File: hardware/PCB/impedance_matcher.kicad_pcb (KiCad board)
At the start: 2 copper layers, 72 x 63 mm, 43 parts, among them Q1 PC817, U1 TLV2372IP

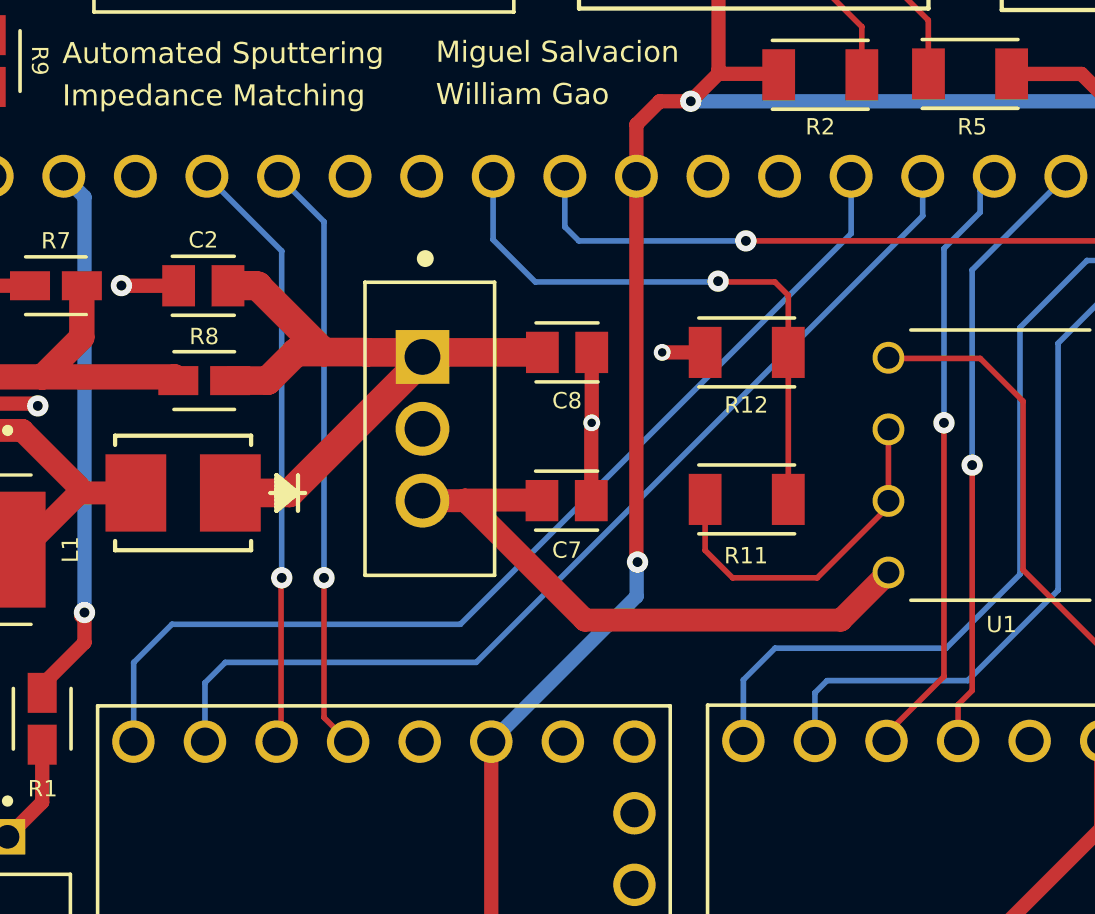
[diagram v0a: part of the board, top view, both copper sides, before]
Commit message: Move capacitor closer to op-amp VDD
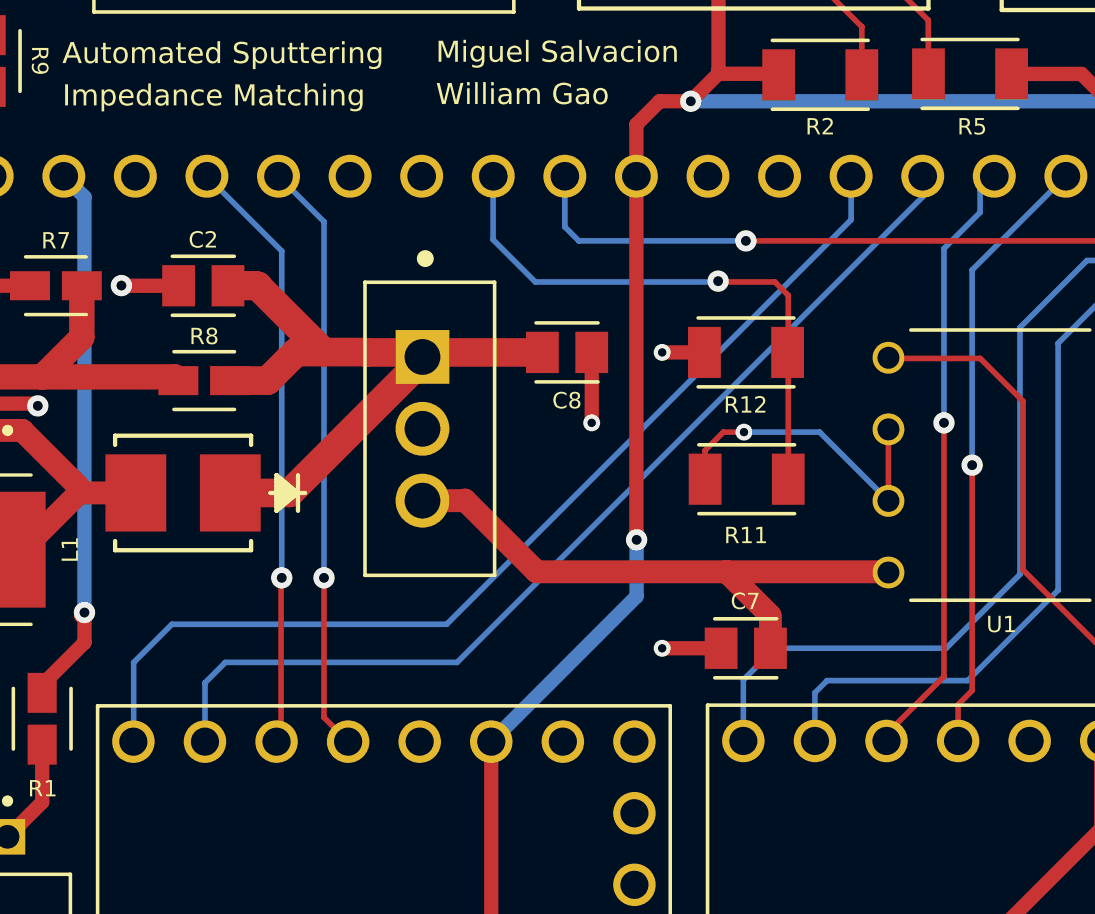
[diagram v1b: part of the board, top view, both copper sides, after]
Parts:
- moved C7 8.24 mm to (69.5, 57.0), turned to 0 degrees
- moved R11 0.72 mm to (69.5, 51.0)
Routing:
- net /IN2: track 12.3 -> 11.3 mm, vias 0 -> 1
- net 12V: track 21.6 -> 20.9 mm
- net GND: track 24.6 -> 24.0 mm, vias 9 -> 10

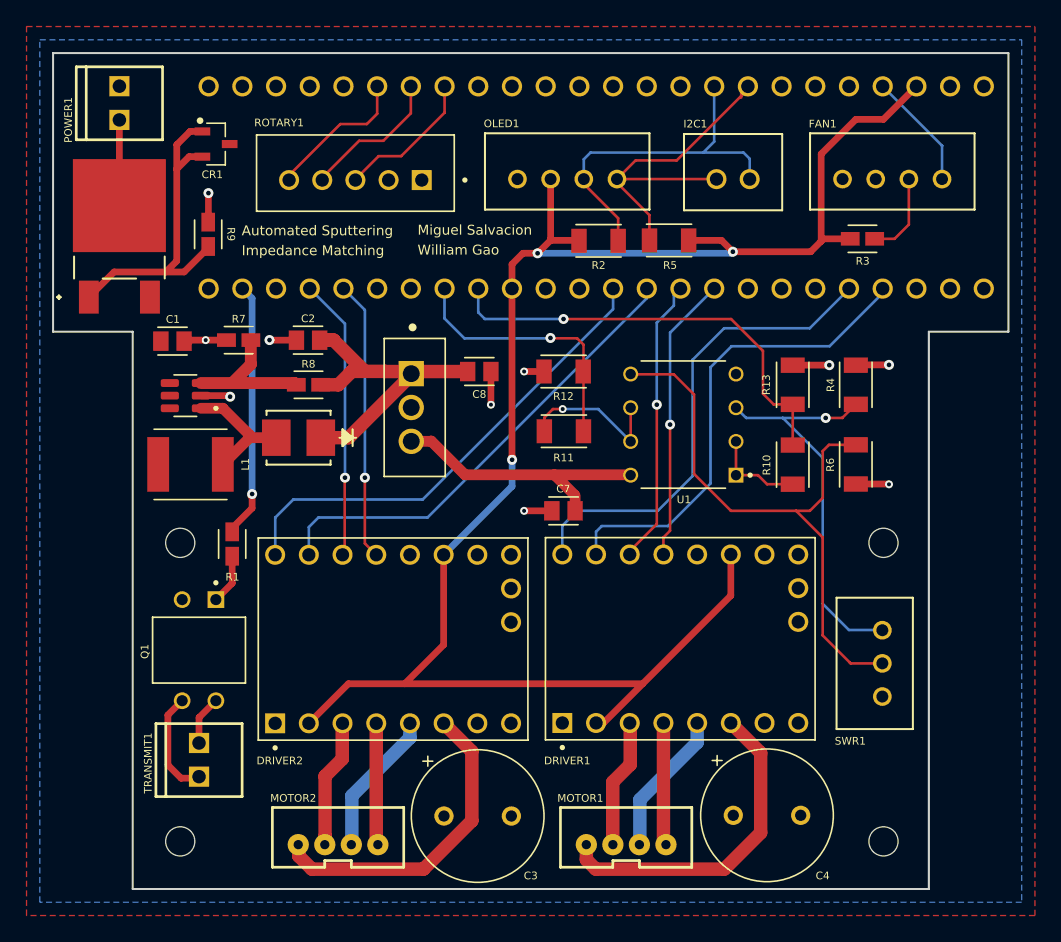
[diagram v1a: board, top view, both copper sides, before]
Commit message: Switch to 4 layer PCB and add ferrite beads
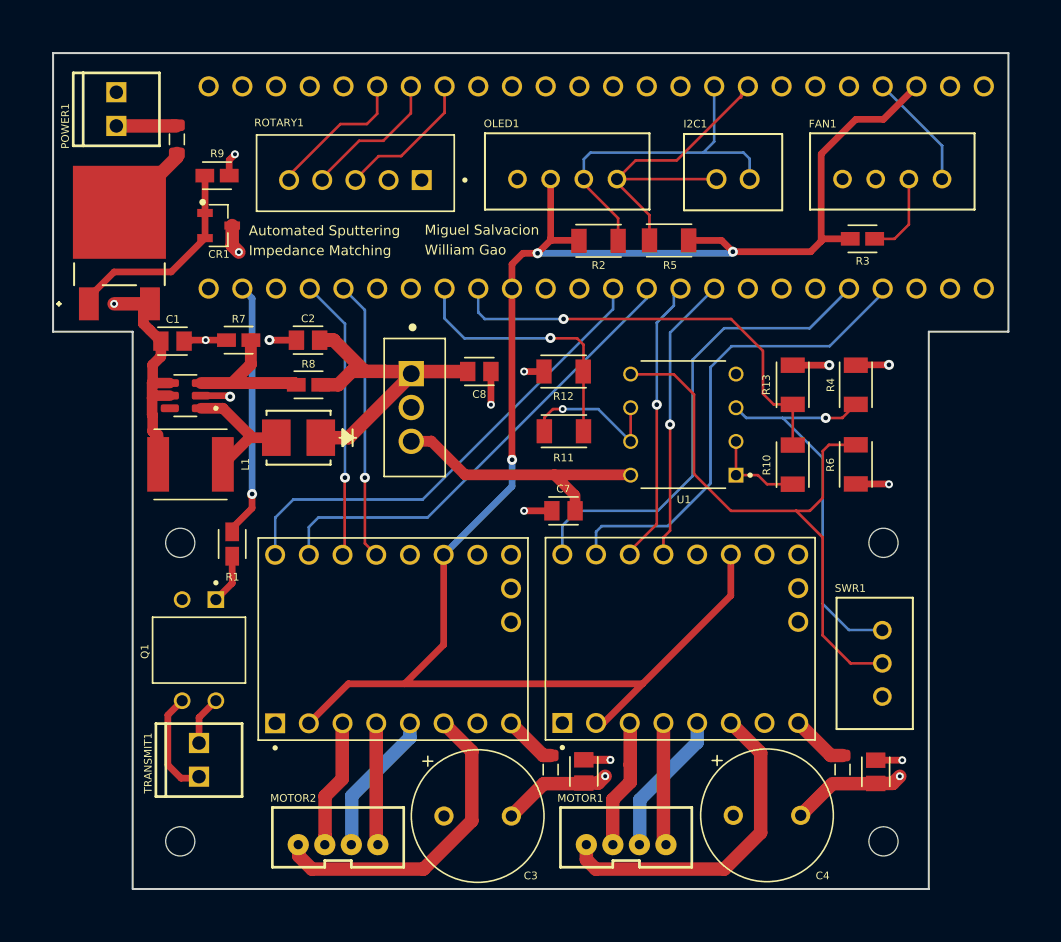
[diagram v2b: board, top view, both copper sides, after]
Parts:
- added C10: 330n, Capacitor:CAPC2012X110, F.Cu at (71.0, 76.6)
- added C9: 330n, Capacitor:CAPC2012X110, F.Cu at (93.0, 76.7)
- added FB1: FerriteBead, Inductor_SMD:L_0805_2012Metric, F.Cu at (40.3, 29.0)
- added FB2: FerriteBead, Inductor_SMD:L_0805_2012Metric, F.Cu at (90.5, 76.5)
- added FB3: FerriteBead, Inductor_SMD:L_0805_2012Metric, F.Cu at (68.5, 76.5)
- CR1: value BZX84B24-E3-08SOT-23_2P9X1P3-1P9_VIS -> BZX84C5V6
- moved CR1 6.15 mm to (43.5, 35.5)
- moved R9 4.47 mm to (43.4, 31.7), turned to 180 degrees
- moved POWER1 0.51 mm to (35.8, 28.0)
- moved REV_POLARITY1 0.50 mm to (36.0, 36.8)
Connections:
- DRIVER1 pad 8: 5V -> Net-(DRIVER1-VM)
- DRIVER2 pad 8: 5V -> Net-(DRIVER2-VM)
- REV_POLARITY1 pad 3: Net-(POWER1-Pin_2) -> Net-(FB1-Pad2)
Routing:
- net 5V: track 0.00 -> 36.7 mm, vias 0 -> 4
- net Net-(CR1-Pad1): track 25.1 -> 15.3 mm
- net Net-(FB1-Pad2): track 0.00 -> 6.16 mm
- net Net-(DRIVER1-VM): track 0.00 -> 4.35 mm
- net Net-(DRIVER2-VM): track 0.00 -> 3.99 mm
- net GND: track 24.0 -> 27.6 mm, vias 10 -> 12
- net Net-(POWER1-Pin_2): track 6.46 -> 4.51 mm
- added copper zone on In2.Cu, net 5V
- added copper zone on In1.Cu, net GND
- removed copper zone on F.Cu, net 5V
- removed copper zone on B.Cu, net GND
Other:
- copper layers 2 -> 4

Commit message: Switch all resistors to 0805
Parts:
- R10, R11, R12, R13, R2, R4, R5, R6: footprint Resistor:RESC3216X70 -> Resistor:RESC2012X65
- moved C10 0.50 mm to (71.5, 76.6)
- moved FB3 0.50 mm to (69.0, 76.5)
- moved FB2 0.36 mm to (90.9, 76.5)
- moved C9 0.36 mm to (93.4, 76.7)
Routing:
- net GND: track 27.6 -> 22.3 mm, vias 12 -> 11
- net /REV_OUT: track 20.9 -> 19.4 mm
- net /IN2: track 11.3 -> 10.2 mm, vias 1 -> 0
- net 3.3V: track 132.6 -> 133.8 mm
- net /REV_IN: track 44.5 -> 43.6 mm
- net /FWD_IN: track 30.3 -> 31.2 mm
- net /SCL: track 26.5 -> 27.1 mm
